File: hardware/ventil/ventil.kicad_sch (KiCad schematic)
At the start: 32 parts, among them J1 Conn_01x05_Pin, J2 M, J3 BUS, J4 i2C, Q1 BSS123, U1 SHT31-DIS, U2 PIC18F05Q40, U4 MCP2003B, U5 uA7805, U6 ULN2003

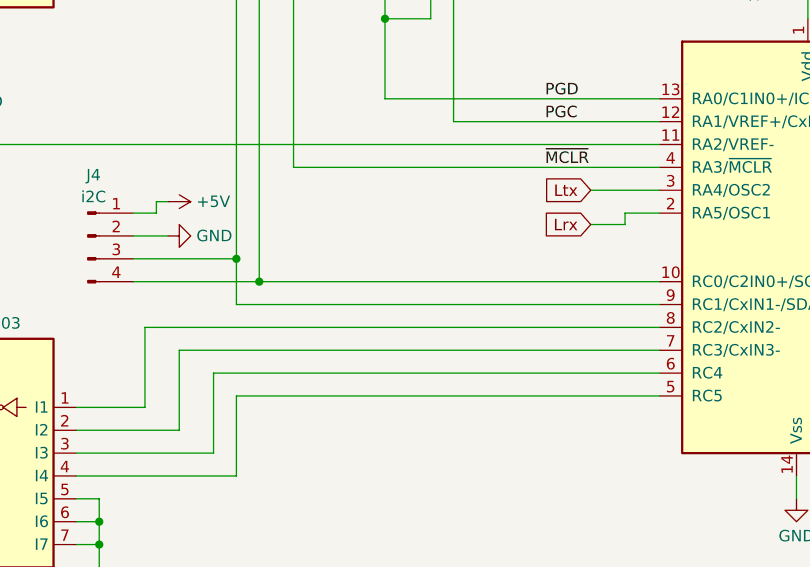
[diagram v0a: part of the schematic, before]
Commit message: hardware/ventil: name SCL/SDA
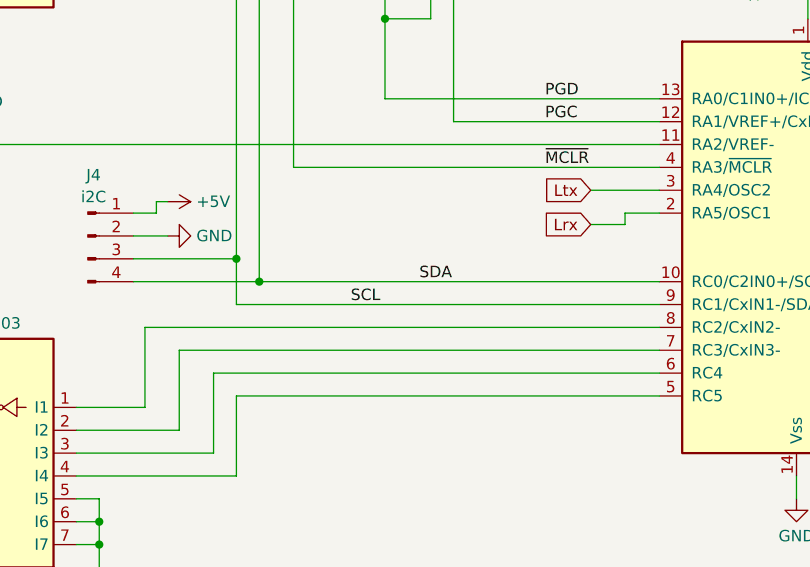
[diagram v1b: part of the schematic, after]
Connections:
- net SCL: now reaches J4.3 (Pin_3), R3.1, U1.4 (SCL), U2.9 (RC1/CxIN1-/SDA)
- net SDA: now reaches J4.4 (Pin_4), R2.1, U1.1 (SDA), U2.10 (RC0/C2IN0+/SCL)
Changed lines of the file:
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@@
+		)
+	)
+	(label "SCL"
+		(at 186.69 80.01 0)
+		(fields_autoplaced yes)
+		(effects
+			(font
+				(size 1.27 1.27)
+			)
+			(justify left bottom)
 		)
 	)
@@
 		(fields_autoplaced yes)
 		(effects
+			(font
+				(size 1.27 1.27)
+			)
+			(justify left bottom)
+		)
+	)
+	(label "SDA"
+		(at 194.31 77.47 0)
+		(fields_autoplaced yes)
+		(effects
